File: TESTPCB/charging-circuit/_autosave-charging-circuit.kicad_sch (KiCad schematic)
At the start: 232 parts, among them J1 2.54-1*6PHeader-RA, J10 Conn_01x02, J11 Conn_01x04, J2 USB_C_Receptacle_PowerOnly_6P, P1 Header-Male-2.54_2x2, P10 1.27mm/1*3p, P11 1.27mm/1*3p, P2 Header-Male-2.54_2x2, P3 1.27mm/1*3p, P4 1.27mm/1*3p, P5 1.27mm/1*3p, P6 1.27mm/1*3p, P7 1.27mm/1*3p, P8 1.27mm/1*3p, P9 1.27mm/1*3p, Q1 2N7002, Q10 AO3400A, Q11 AO3401A, Q2 CJQ4435, Q3 currentmirror, Q4 BSS84, Q5 AO4892, Q6 AO3401A, Q7 AO3401A, Q8 CJQ4435, Q9 AO3400A, SW1 TS-1088R-02026, U1 MAX17048G+T10, U10 BQ25606RGER, U11 Battery Input, U12 BQ24170RGYR, U13 TPS54302DDCR_C311983, U14 NTC10K/0805/F, U15 BQ76920PW, U16 NTC10K/0805/F, U17 HUSB238_002DD, U19 TPS54302DDCR_C311983, U2 MT3608, U20 TPS54302DDCR_C311983, U21 MCP73871, U3 MT3608, U4 TPL5110DDCT, U5 BQ25606RGER, U6 MT3608, U7 Z-21320110021001, U8 MAX3232CDBR, U9 ADS1115IDGSR

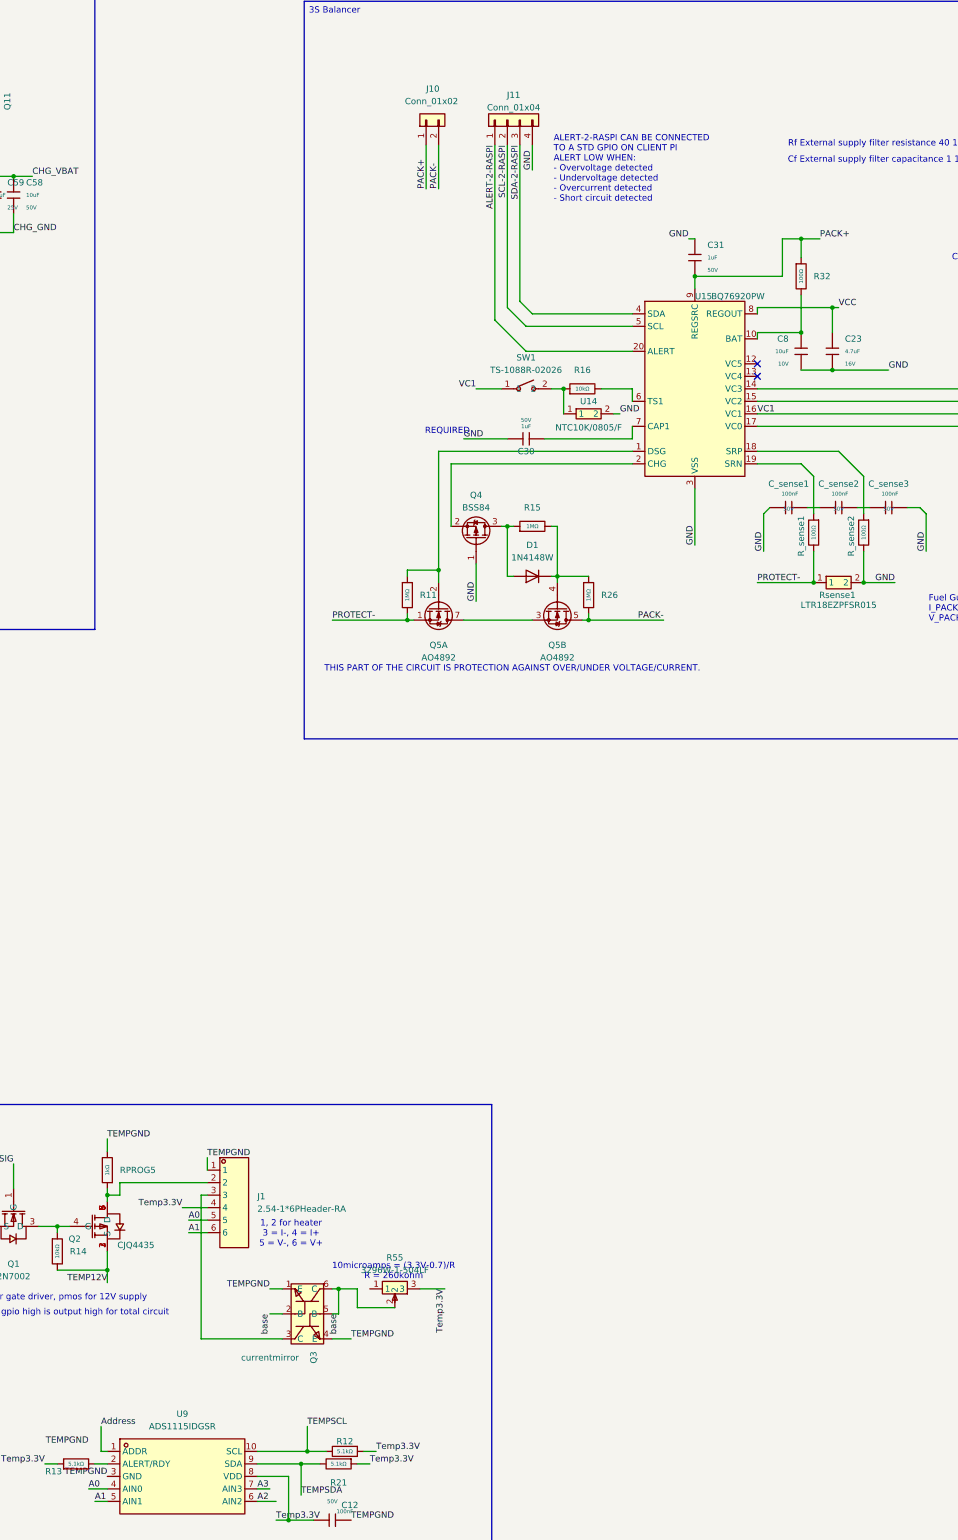
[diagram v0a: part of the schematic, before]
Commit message: Finished Traces and Aligned Modules, Just need to do Mousebites
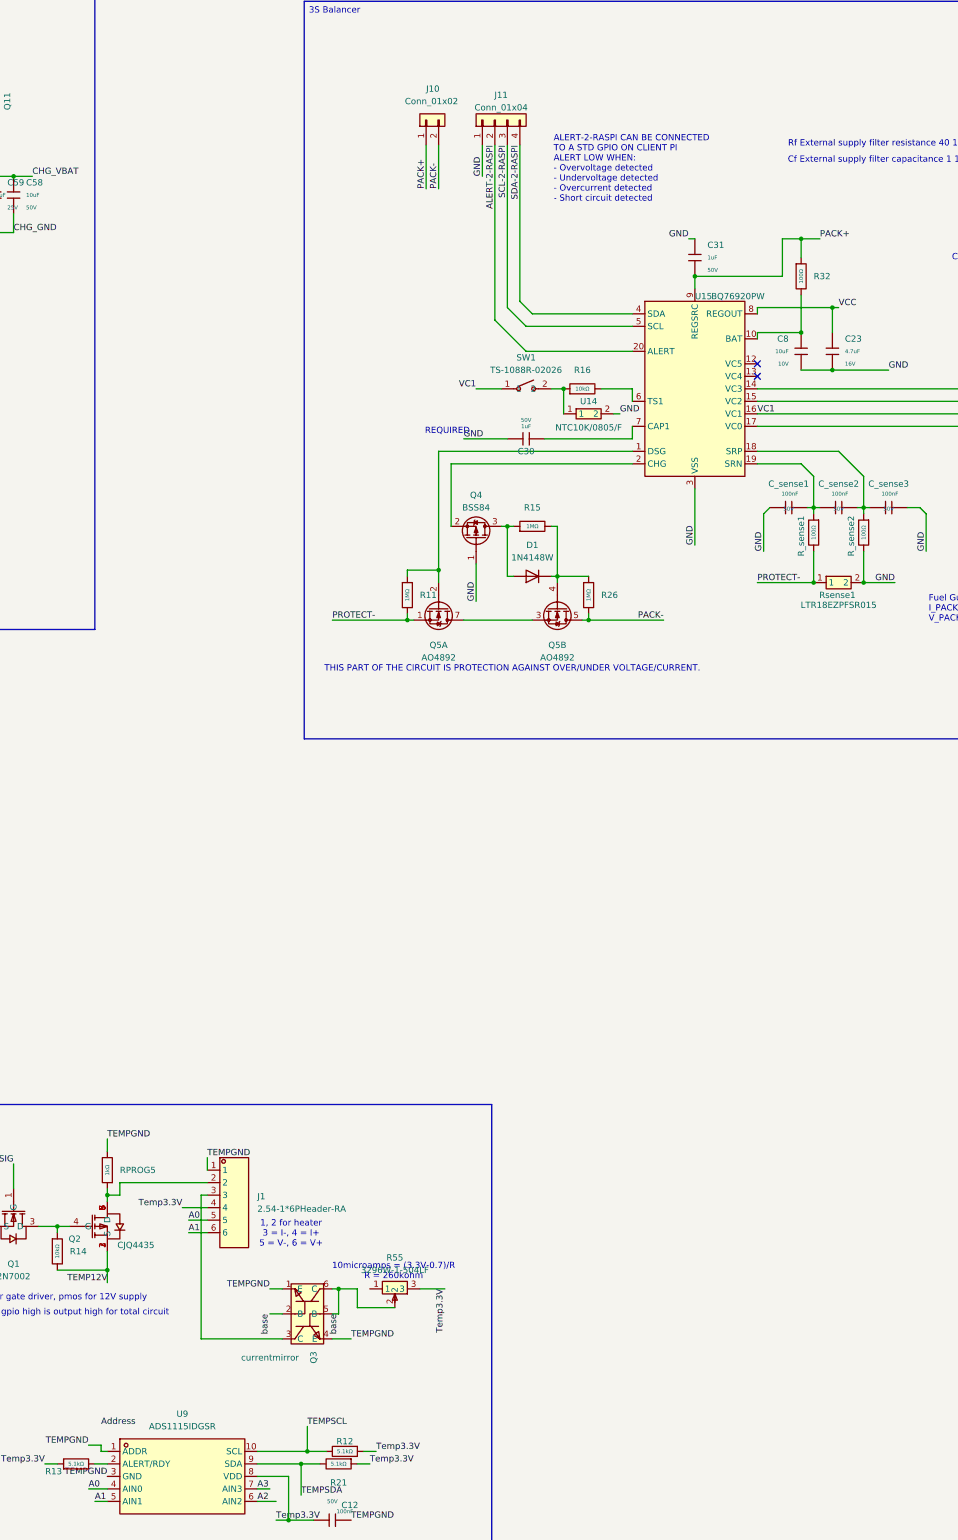
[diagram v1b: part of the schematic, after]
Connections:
- net ALERT-2-RASPI: now also J11.2 (Pin_2); no longer J11.1 (Pin_1)
- net Address: no longer U9.1 (ADDR)
- net BAT_3 (-): now also J11.1 (Pin_1); no longer J11.4 (Pin_4)
- net SCL-2-RASPI: now also J11.3 (Pin_3); no longer J11.2 (Pin_2)
- net SDA-2-RASPI: now also J11.4 (Pin_4); no longer J11.3 (Pin_3)
- net TEMPGND: now also U9.1 (ADDR)
- net at C_sense1.2, C_sense2.1: now also R_sense1.1, U15.19 (SRN)
- net at C_sense2.2, C_sense3.1: now also R_sense2.1, U15.18 (SRP)
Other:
- moved on the sheet: J11
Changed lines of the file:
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@@
 	)
 	(junction
+		(at 504.19 -90.17)
+		(diameter 0)
+		(color 0 0 0 0)
+	)
+	(junction
 		(at 267.97 -189.23)
 		(diameter 0)
@@
 	)
 	(junction
+		(at 514.35 -90.17)
+		(diameter 0)
+		(color 0 0 0 0)
+	)
+	(junction
 		(at 218.44 -189.23)
 		(diameter 0)
@@
 	(wire
 		(pts
-			(xy 447.04 -163.83) (xy 447.04 -158.75)
-		)
-		(stroke
-			(width 0)
-			(type default)
-		)
-	)
-	(wire
-		(pts
 			(xy 205.74 -132.08) (xy 205.74 -119.38)
 		)
@@
 	(wire
 		(pts
-			(xy 502.92 -90.17) (xy 505.46 -90.17)
+			(xy 502.92 -90.17) (xy 504.19 -90.17)
 		)
 		(stroke
@@
 	(wire
 		(pts
+			(xy 439.42 -163.83) (xy 439.42 -128.27)
+		)
+		(stroke
+			(width 0)
+			(type default)
+		)
+	)
+	(wire
+		(pts
 			(xy 259.08 -102.87) (xy 260.35 -102.87)
 		)
@@
 	(wire
 		(pts
+			(xy 514.35 -90.17) (xy 515.62 -90.17)
+		)
+		(stroke
+			(width 0)
+			(type default)
+		)
+	)
+	(wire
+		(pts
 			(xy 307.34 -127) (xy 308.61 -127)
 		)
@@
 	(wire
 		(pts
-			(xy 439.42 -163.83) (xy 439.42 -128.27)
-		)
-		(stroke
-			(width 0)
-			(type default)
-		)
-	)
-	(wire
-		(pts
 			(xy -142.24 -151.13) (xy -137.16 -151.13)
 		)
@@
 	(wire
 		(pts
+			(xy 514.35 -90.17) (xy 514.35 -88.9)
+		)
+		(stroke
+			(width 0)
+			(type default)
+		)
+	)
+	(wire
+		(pts
 			(xy 266.7 -90.17) (xy 267.97 -90.17)
 		)
@@
 	(wire
 		(pts
-			(xy 444.5 -163.83) (xy 444.5 -132.08)
-		)
-		(stroke
-			(width 0)
-			(type default)
-		)
-	)
-	(wire
-		(pts
 			(xy 218.44 -189.23) (xy 227.33 -189.23)
 		)
@@
 	(wire
 		(pts
-			(xy 514.35 -96.52) (xy 514.35 -88.9)
+			(xy 514.35 -96.52) (xy 514.35 -90.17)
 		)
 		(stroke
@@
 	(wire
 		(pts
+			(xy 356.87 100.33) (xy 359.41 100.33)
+		)
+		(stroke
+			(width 0)
+			(type default)
+		)
+	)
+	(wire
+		(pts
 			(xy 50.8 48.26) (xy 48.26 48.26)
 		)
@@
 	(wire
 		(pts
+			(xy 359.41 100.33) (xy 359.41 101.6)
+		)
+		(stroke
+			(width 0)
+			(type default)
+		)
+	)
+	(wire
+		(pts
 			(xy 508 -130.81) (xy 508 -125.73)
 		)
@@
 	(wire
 		(pts
+			(xy 444.5 -163.83) (xy 444.5 -132.08)
+		)
+		(stroke
+			(width 0)
+			(type default)
+		)
+	)
+	(wire
+		(pts
 			(xy 100.33 143.51) (xy 100.33 148.59)
 		)
@@
 	(wire
 		(pts
+			(xy 504.19 -90.17) (xy 505.46 -90.17)
+		)
+		(stroke
+			(width 0)
+			(type default)
+		)
+	)
+	(wire
+		(pts
 			(xy 123.19 161.29) (xy 127 161.29)
 		)
@@
 	(wire
 		(pts
-			(xy 504.19 -96.52) (xy 504.19 -88.9)
+			(xy 504.19 -96.52) (xy 504.19 -90.17)
 		)
 		(stroke
@@
 	(wire
 		(pts
-			(xy 441.96 -163.83) (xy 441.96 -130.81)
-		)
-		(stroke
-			(width 0)
-			(type default)
-		)
-	)
-	(wire
-		(pts
 			(xy -187.96 86.36) (xy -185.42 86.36)
 		)
@@
 	(wire
 		(pts
-			(xy 359.41 96.52) (xy 359.41 101.6)
-		)
-		(stroke
-			(width 0)
-			(type default)
-		)
-	)
-	(wire
-		(pts
 			(xy -152.4 -135.89) (xy -152.4 -123.19)
 		)
@@
 	(wire
 		(pts
-			(xy 513.08 -90.17) (xy 515.62 -90.17)
+			(xy 513.08 -90.17) (xy 514.35 -90.17)
 		)
 		(stroke
@@
 	(wire
 		(pts
+			(xy 504.19 -90.17) (xy 504.19 -88.9)
+		)
+		(stroke
+			(width 0)
+			(type default)
+		)
+	)
+	(wire
+		(pts
 			(xy 360.68 64.77) (xy 360.68 67.31)
 		)
@@
 	(wire
 		(pts
+			(xy 436.88 -163.83) (xy 436.88 -157.48)
+		)
+		(stroke
+			(width 0)
+			(type default)
+		)
+	)
+	(wire
+		(pts
 			(xy 334.01 -151.13) (xy 334.01 -116.84)
 		)
@@
 	(wire
 		(pts
+			(xy 441.96 -163.83) (xy 441.96 -130.81)
+		)
+		(stroke
+			(width 0)
+			(type default)
+		)
+	)
+	(wire
+		(pts
 			(xy -82.55 201.93) (xy -80.01 201.93)
 		)
@@
 	)
 	(label "GND"
-		(at 447.04 -158.75 90)
+		(at 436.88 -157.48 90)
 		(effects
 			(font
@@
 	(symbol
 		(lib_id "Connector_Generic:Conn_01x04")
-		(at 441.96 -168.91 90)
+		(at 439.42 -168.91 90)
 		(unit 1)
 		(exclude_from_sim no)
@@
 		(fields_autoplaced yes)
 		(property "Reference" "J11"
-			(at 443.23 -173.99 90)
+			(at 440.69 -173.99 90)
 			(effects
 				(font
@@
 		)
 		(property "Value" "Conn_01x04"
-			(at 443.23 -171.45 90)
+			(at 440.69 -171.45 90)
 			(effects
 				(font
@@
 		)
 		(property "Footprint" "Connector_PinHeader_2.54mm:PinHeader_1x04_P2.54mm_Vertical"
-			(at 441.96 -168.91 0)
+			(at 439.42 -168.91 0)
 			(effects
 				(font
@@
 		)
 		(property "Datasheet" "~"
-			(at 441.96 -168.91 0)
+			(at 439.42 -168.91 0)
 			(effects
 				(font
@@
 		)
 		(property "Description" "Generic connector, single row, 01x04, script generated (kicad-library-utils/schlib/autogen/connector/)"
-			(at 441.96 -168.91 0)
+			(at 439.42 -168.91 0)
 			(effects
 				(font
@@
 		)
 		(property "LCSC Part" "C5116483"
-			(at 441.96 -168.91 90)
+			(at 439.42 -168.91 90)
 			(effects
 				(font
